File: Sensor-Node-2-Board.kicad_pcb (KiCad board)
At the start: 2 copper layers, 100 x 100 mm, 67 parts, among them J401 EBWA-02-B, J701 PS0519, J702 EBWA-02-B, Q101 BC549, Q401 Si4944DY, SW501 SW_HELP, U201 LM393, U601 Photon 2, U701 L7805

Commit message: fix: pcb dimensioning
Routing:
- net /SCHEMATIC/FAN-: track 20.9 -> 19.9 mm
- net +12V: track 109.5 -> 108.5 mm
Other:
- board text added: "2026"
- board text added: "A"
- board text added: "FAN SPEED OVRD"
- board text added: "HELP BUTTON"
- board text added: "MIC"
- board text added: "REV"
- board text added: "SENSITIVITY"
- board text added: "SN2 BREAKOUT BOARD"
- board text added: "STATUS"
- board text removed: "30°"

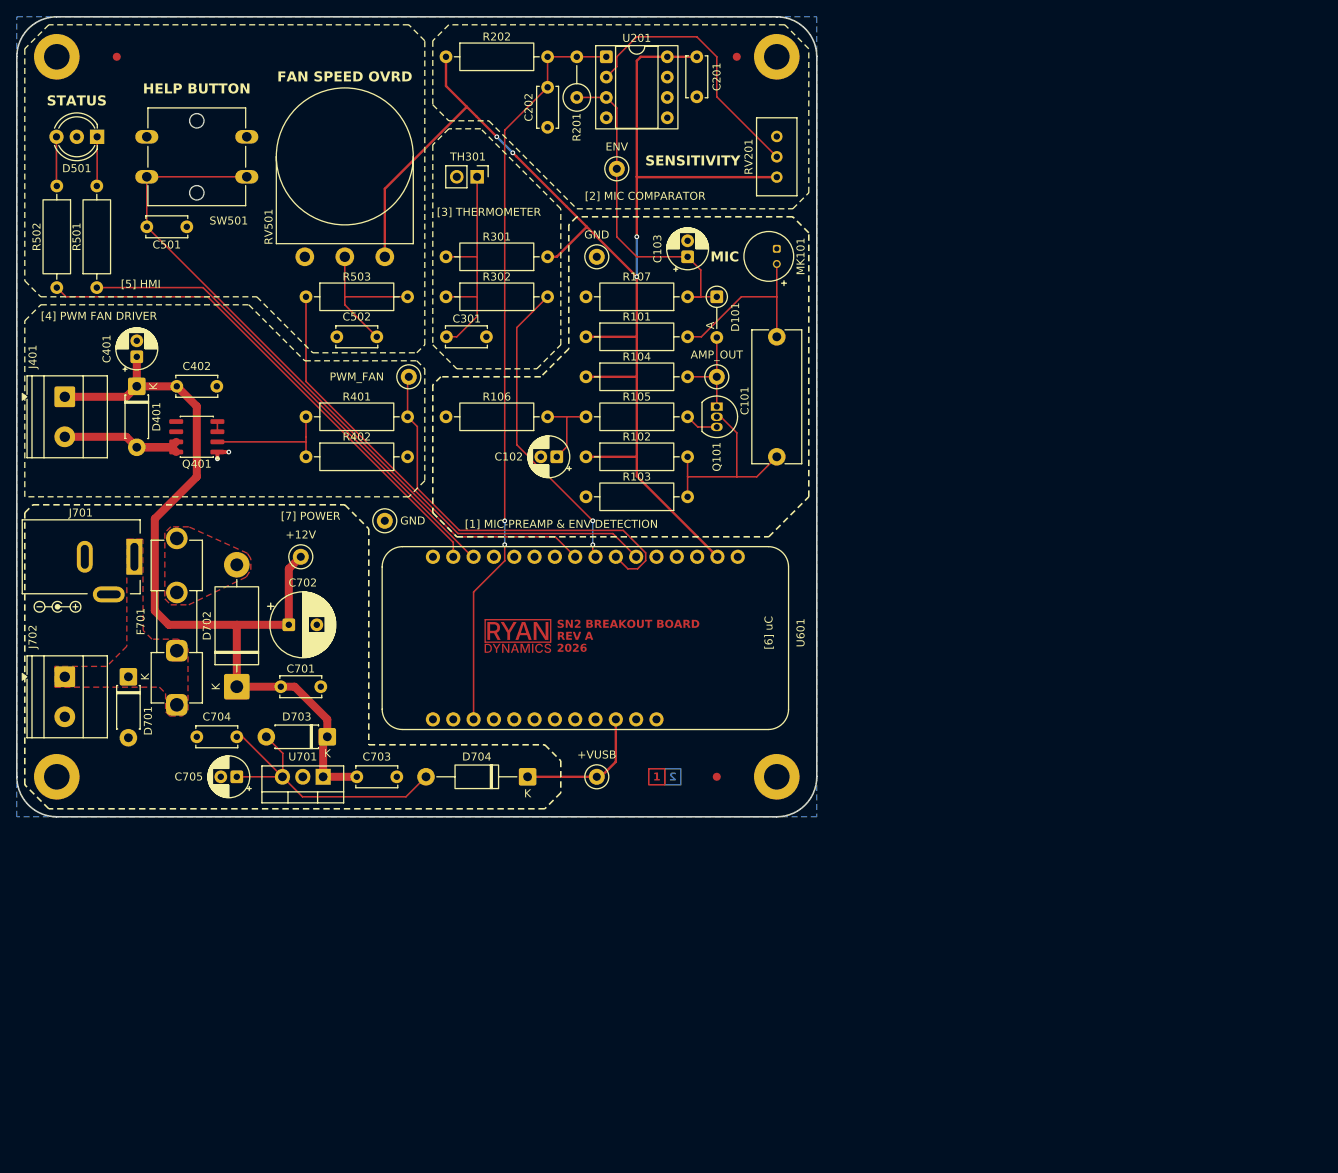
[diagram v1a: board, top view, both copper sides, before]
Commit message: fix: pcb fab/assembly doc layout
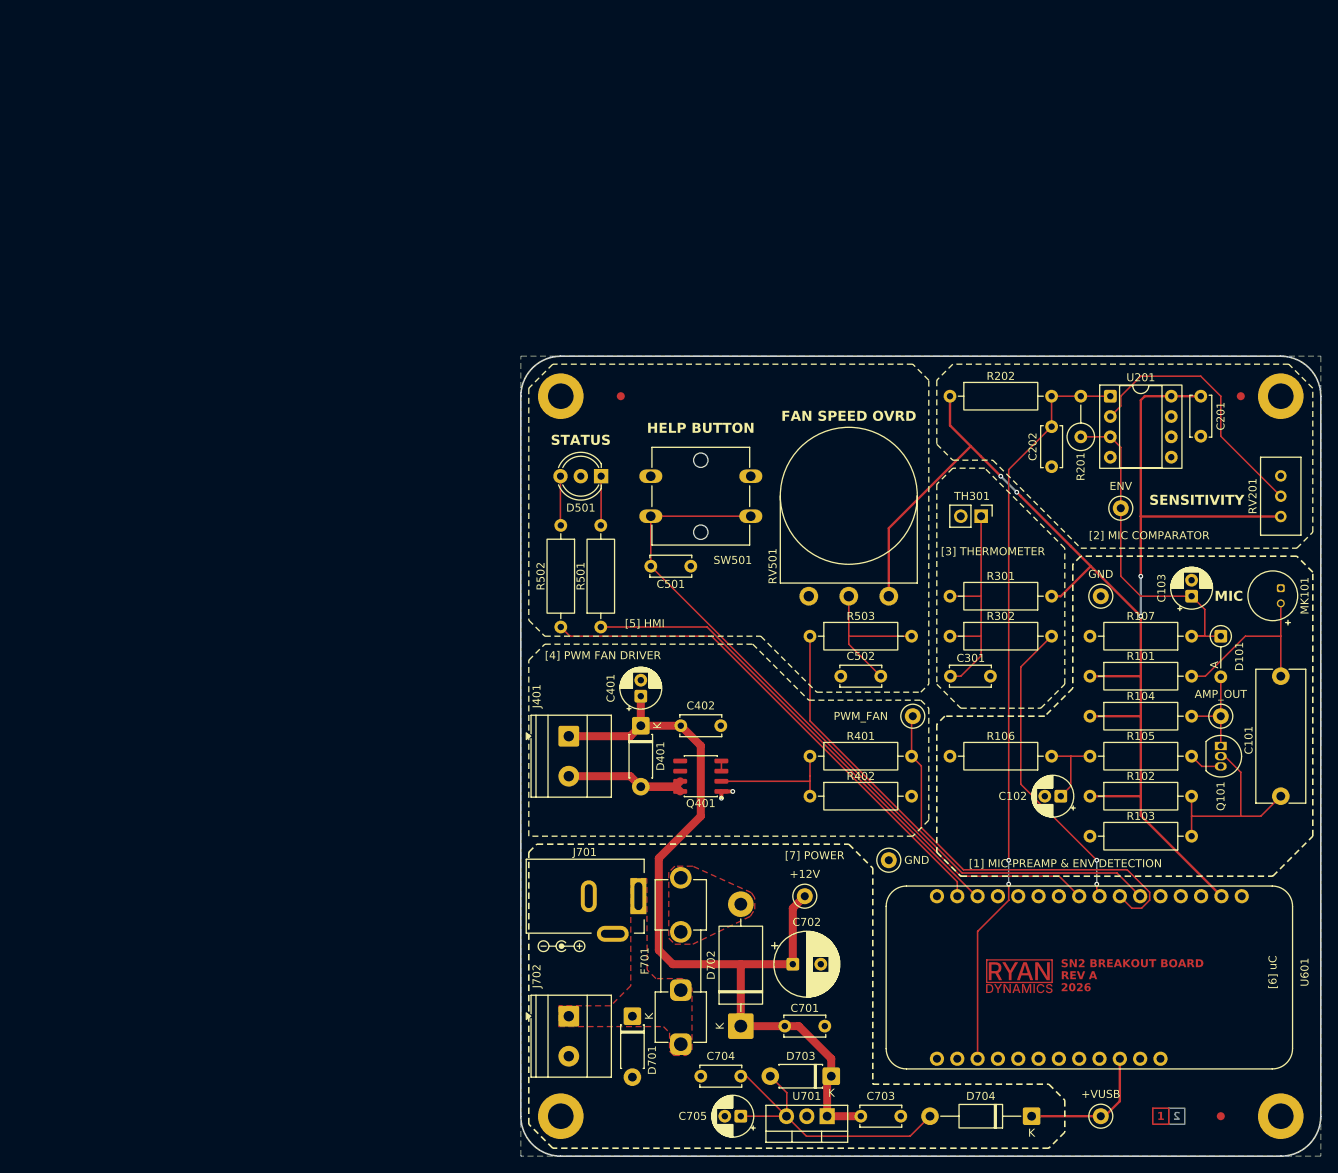
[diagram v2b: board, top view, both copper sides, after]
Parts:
- moved C101 76.0 mm to (260.0, 112.4)
- moved C102 76.0 mm to (232.5, 127.4)
- moved C103 76.0 mm to (248.8, 102.4)
- moved C201 76.0 mm to (250.0, 77.4)
- moved C202 76.0 mm to (231.3, 81.2)
- moved C301 76.0 mm to (218.7, 112.4)
- moved C401 76.0 mm to (180.0, 114.9)
- moved C402 76.0 mm to (185.0, 118.6)
- moved C501 76.0 mm to (181.2, 98.7)
- moved C502 76.0 mm to (205.0, 112.4)
- moved C701 76.0 mm to (203.0, 156.2)
- moved C702 76.0 mm to (199.0, 148.4)
- moved C703 76.0 mm to (212.5, 167.4)
- moved C704 76.0 mm to (187.5, 162.4)
- moved C705 76.0 mm to (192.5, 167.4)
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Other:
- board text removed: "3× 120°"
